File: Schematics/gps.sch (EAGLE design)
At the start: 23 parts, among them IC1 74HC14D, Q1 PE4259, Q2 MIC5365, U1 NEO-8Q, X1 REF_DC, X2 REF_AC

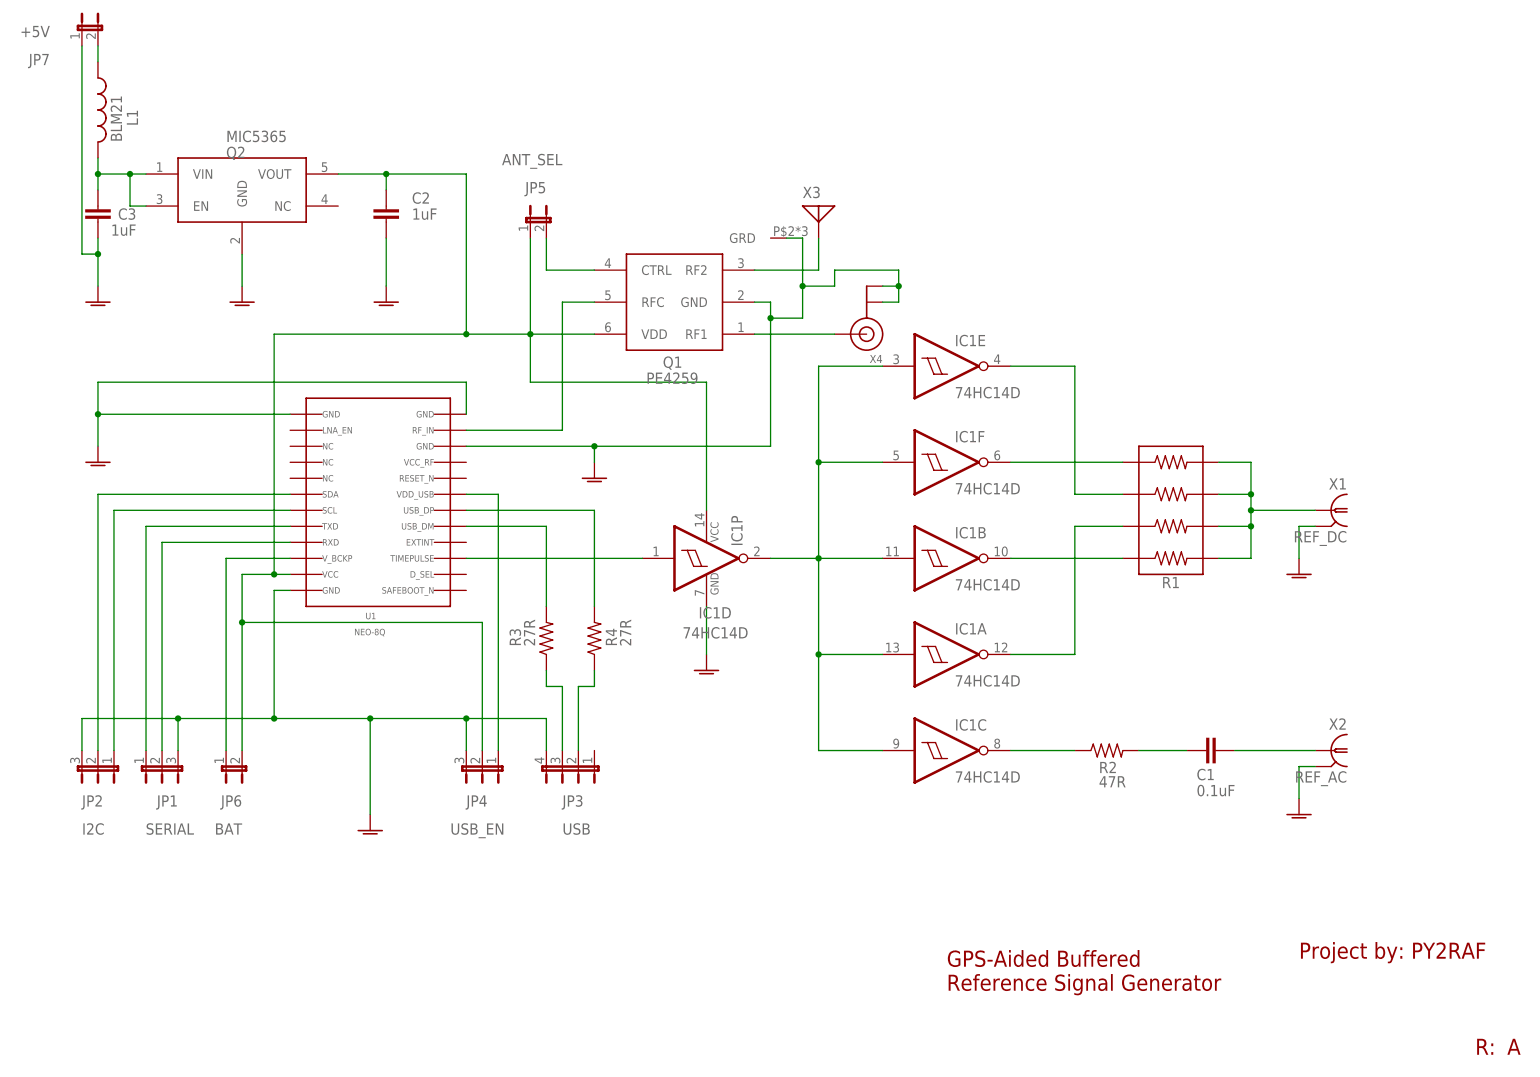
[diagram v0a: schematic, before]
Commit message: New GPS version: Now feeding a Si5351
Test version.
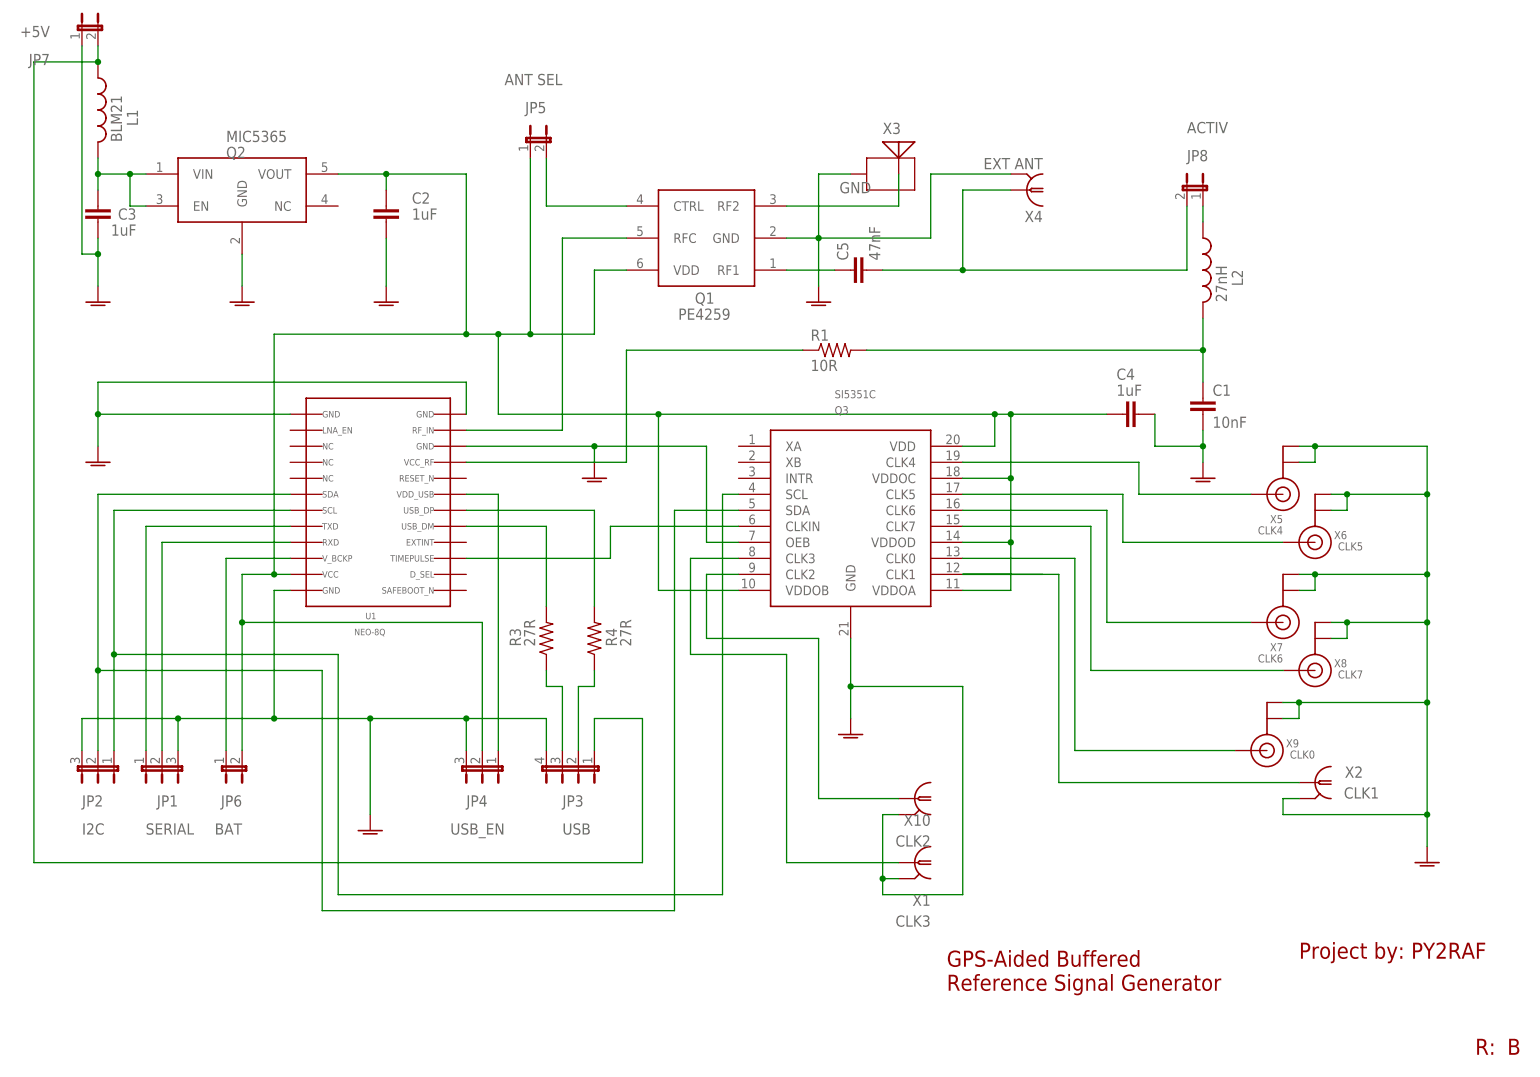
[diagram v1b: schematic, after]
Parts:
- removed IC1: 74HC14D, 74xx-eu:74HC14D
- removed R2: 47R, rcl:R-US_M1206
- added C4: 1uF, rcl:C-EUC1206
- added C5: 47nF, rcl:C-EUC0805K
- added JP8: ACTIV, jumper:JP1E
- added L2: 27nH, aarf:L-0805
- added Q3: SI5351C, aarf:SI5351C
- added X10: CLK2, aarf:SMA-PCB
- added X5: CLK4, adafruit:ANTENNA_U.FL
- added X6: CLK5, adafruit:ANTENNA_U.FL
- added X7: CLK6, adafruit:ANTENNA_U.FL
- added X8: CLK7, adafruit:ANTENNA_U.FL
- added X9: CLK0, adafruit:ANTENNA_U.FL
- C1: value 0.1uF -> 10nF; device rcl:C-EUC1206 -> rcl:C-EUC0805K
- JP5: value ANT_SEL -> ANT SEL
- R1: value (none) -> 10R; device aarf:744C083 -> rcl:R-US_R0805
- X1: value REF_DC -> CLK3
- X2: value REF_AC -> CLK1
- X4: value (none) -> EXT ANT; device adafruit:ANTENNA_U.FL -> aarf:SMA-PCB
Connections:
- removed net N$4: IC1B.O, R1.1
- new net N$28: JP3.1, JP7.2, L1.1
- new net N$29: Q3.CLK7, X8.SIGNAL
- new net N$30: Q3.CLK0, X9.SIGNAL
- new net N$31: Q3.CLK3, X1.1
- net GNDA: now also C1.2, C4.2, Q3.GND, Q3.OEB, X10.2, X4.2, X5.GND@0, X5.GND@1, X6.GND@0, X6.GND@1, X7.GND@0, X7.GND@1, X8.GND@0, X8.GND@1, X9.GND@0, X9.GND@1; no longer IC1P.GND, X4.GND@0, X4.GND@1
- net N$1: now also Q3.CLKIN, U1.P$3; no longer IC1A.I, IC1B.I, IC1C.I, IC1D.O, IC1E.I, IC1F.I
- net N$11: now also JP8.1, L2.1; no longer C1.1, X2.1
- net N$15: now also Q3.SDA
- net N$16: now also Q3.SCL
- net N$2: now also Q3.CLK1, X2.1; no longer IC1E.O, R1.3
- net N$21: now also Q3.CLK4, X5.SIGNAL; no longer R1.5, R1.6, R1.7, R1.8, X1.1
- net N$22: now also C4.1, Q3.VDD, Q3.VDDOA, Q3.VDDOB, Q3.VDDOC, Q3.VDDOD; no longer IC1P.VCC
- net N$25: now also Q3.CLK5, X6.SIGNAL; no longer JP7.2, L1.1
- net N$27: now also Q3.CLK6, X7.SIGNAL; no longer Q1.RF1, X4.SIGNAL
- net N$3: now also Q3.CLK2, X10.1; no longer IC1A.O, R1.2
- net N$5: now also C5.2, JP8.2, X4.1; no longer IC1F.O, R1.4
- net N$6: now also C5.1, Q1.RF1; no longer IC1D.I, U1.P$3
- net N$7: now also R1.1, U1.P$9; no longer IC1C.O, R2.1
- net N$8: now also C1.1, L2.2, R1.2; no longer C1.2, R2.2
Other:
- moved on the sheet: C1, JP5, Q1, X1, X2

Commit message: Rev. B: Pull-up in I2C, new GPS Clock port
* Implemented I²C pull-up resistors (required by datasheet)
* Added a U.FL connector in the GPS clock port that drives the 5351 in
  for test / troubleshoot
* Added schematic, gerber, pictures
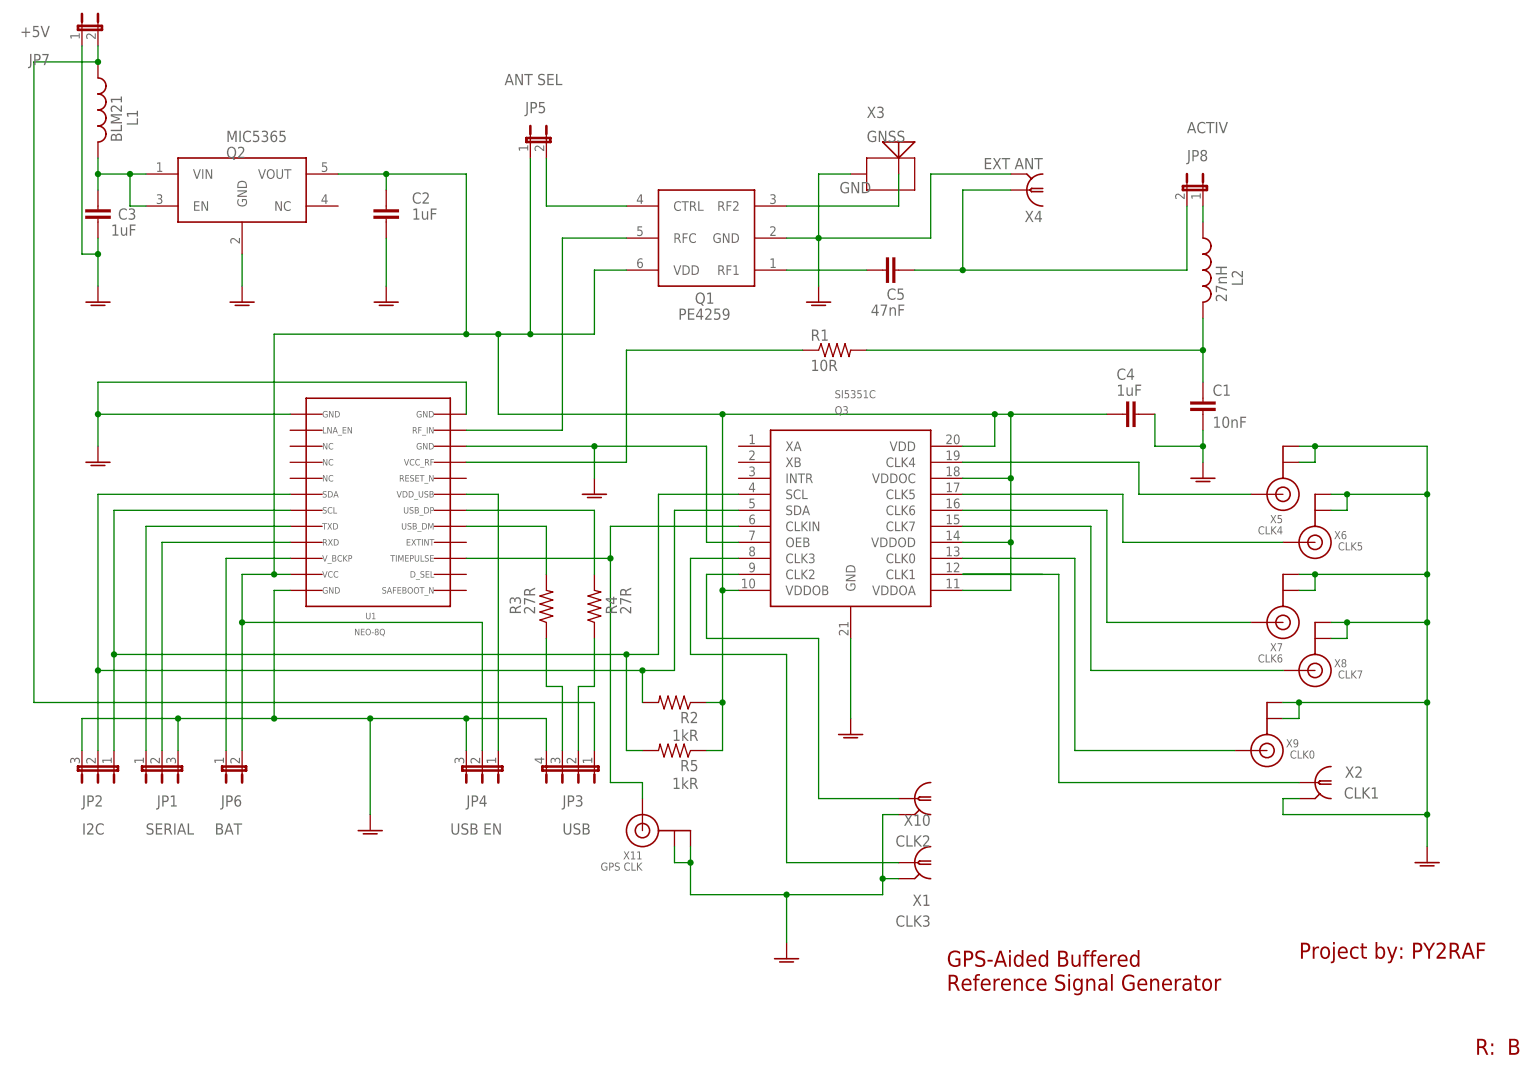
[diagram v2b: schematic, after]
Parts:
- added R2, R5: 1kR, rcl:R-US_R1206
- added X11: GPS CLK, adafruit:ANTENNA_U.FL
- JP4: value USB_EN -> USB EN
- X3: value (none) -> GNSS
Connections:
- net GNDA: now also X11.GND@0, X11.GND@1
- net N$1: now also X11.SIGNAL
- net N$15: now also R2.2
- net N$16: now also R5.2
- net N$22: now also R2.1, R5.1
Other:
- moved on the sheet: C5, R3, R4

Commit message: GPS board: I2C changes
* Separated to two independent I2C ports, one for the uBlox, other for
  the 5351
* Minor re-routing
* Updated BOM, schematics and stuff
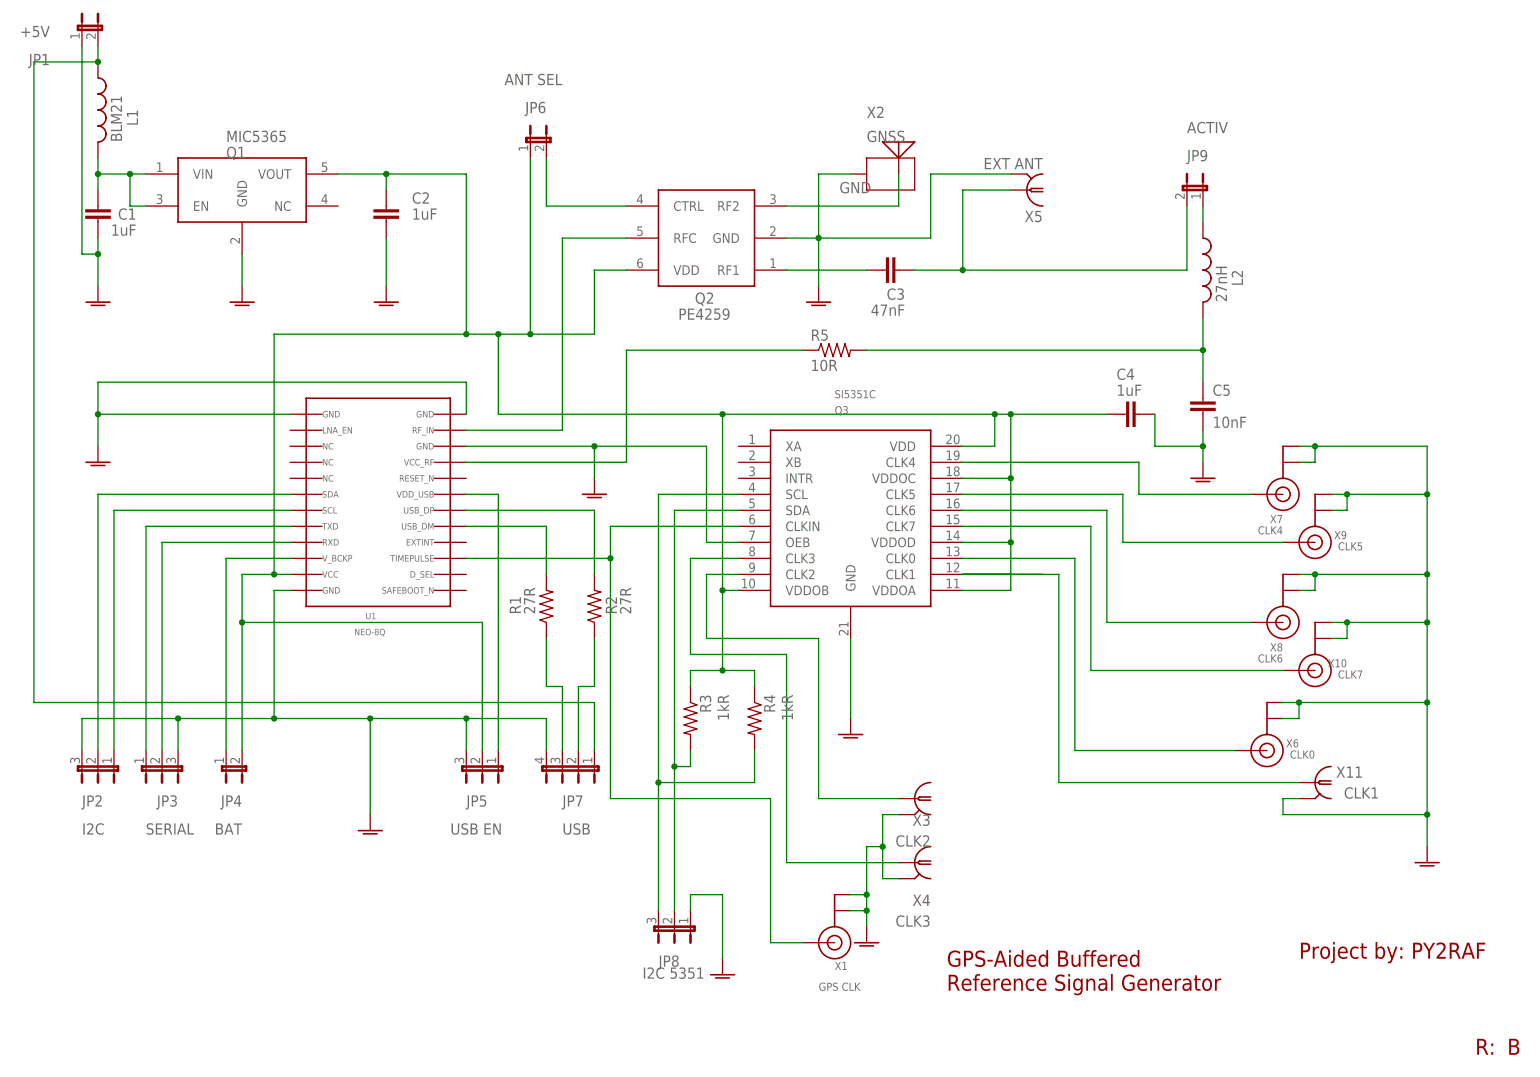
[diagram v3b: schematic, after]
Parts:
- added JP9: ACTIV, jumper:JP1E
- C1: value 10nF -> 1uF; device rcl:C-EUC0805K -> rcl:C-EUC1206
- C3: value 1uF -> 47nF; device rcl:C-EUC1206 -> rcl:C-EUC0805K
- C5: value 47nF -> 10nF
- JP1: value SERIAL -> +5V; device jumper:JP2E -> jumper:JP1E
- JP3: value USB -> SERIAL; device jumper:JP4E -> jumper:JP2E
- JP4: value USB EN -> BAT; device jumper:JP2E -> jumper:JP1E
- JP5: value ANT SEL -> USB EN; device jumper:JP1E -> jumper:JP2E
- JP6: value BAT -> ANT SEL
- JP7: value +5V -> USB; device jumper:JP1E -> jumper:JP4E
- JP8: value ACTIV -> I2C 5351; device jumper:JP1E -> jumper:JP2E
- Q1: value PE4259 -> MIC5365; device aarf:PE4259 -> aarf:MIC5365
- Q2: value MIC5365 -> PE4259; device aarf:MIC5365 -> aarf:PE4259
- R1: value 10R -> 27R; device rcl:R-US_R0805 -> rcl:R-US_M1206
- R2: value 1kR -> 27R; device rcl:R-US_R1206 -> rcl:R-US_M1206
- R3, R4: value 27R -> 1kR; device rcl:R-US_M1206 -> rcl:R-US_R1206
- R5: value 1kR -> 10R; device rcl:R-US_R1206 -> rcl:R-US_R0805
- X1: value CLK3 -> GPS CLK; device aarf:SMA-PCB -> adafruit:ANTENNA_U.FL
- X10: value CLK2 -> CLK7; device aarf:SMA-PCB -> adafruit:ANTENNA_U.FL
- X11: value GPS CLK -> CLK1; device adafruit:ANTENNA_U.FL -> aarf:SMA-PCB
- X2: value CLK1 -> GNSS; device aarf:SMA-PCB -> aarf:ANT-GNSS-MLX
- X3: value GNSS -> CLK2; device aarf:ANT-GNSS-MLX -> aarf:SMA-PCB
- X4: value EXT ANT -> CLK3
- X5: value CLK4 -> EXT ANT; device adafruit:ANTENNA_U.FL -> aarf:SMA-PCB
- X6: value CLK5 -> CLK0
- X7: value CLK6 -> CLK4
- X8: value CLK7 -> CLK6
- X9: value CLK0 -> CLK5
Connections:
- new net N$32: JP8.2, Q3.SDA, R3.2
- new net N$4: JP8.3, Q3.SCL, R4.2
- net GNDA: now also C5.2, JP1.1, JP3.3, JP5.3, JP7.4, JP8.1, X1.GND@0, X1.GND@1, X10.GND@0, X10.GND@1, X11.2, X2.GRD, X3.2, X5.2; no longer C3.2, JP1.3, JP3.4, JP4.3, JP7.1, X1.2, X10.2, X11.GND@0, X11.GND@1, X2.2, X3.GRD, X5.GND@0, X5.GND@1
- net N$1: now also X1.SIGNAL; no longer X11.SIGNAL
- net N$10: now also R2.2; no longer R4.2
- net N$11: now also JP9.1; no longer JP8.1
- net N$12: now also JP5.1; no longer JP4.1
- net N$13: now also JP7.3, R1.1; no longer JP3.3, R3.1
- net N$14: now also JP7.2, R2.1; no longer JP3.2, R4.1
- net N$15: no longer Q3.SDA, R2.2
- net N$16: no longer Q3.SCL, R5.2
- net N$17: now also JP3.2; no longer JP1.2
- net N$18: now also JP3.1; no longer JP1.1
- net N$19: now also JP4.1; no longer JP6.1
- net N$2: now also X11.1; no longer X2.1
- net N$20: now also JP6.2, Q2.CTRL; no longer JP5.2, Q1.CTRL
- net N$21: now also X7.SIGNAL; no longer X5.SIGNAL
- net N$22: now also JP5.2, JP6.1, Q1.VOUT, Q2.VDD, R3.1, R4.1; no longer JP5.1, JP6.2, Q1.VDD, Q2.VOUT, R2.1, R5.1
- net N$23: now also Q2.RFC; no longer Q1.RFC
- net N$24: now also C1.1, Q1.EN, Q1.VIN; no longer C3.1, Q2.EN, Q2.VIN
- net N$25: now also X9.SIGNAL; no longer X6.SIGNAL
- net N$26: now also Q2.RF2, X2.ANT; no longer Q1.RF2, X3.ANT
- net N$27: now also X8.SIGNAL; no longer X7.SIGNAL
- net N$28: now also JP1.2, JP7.1; no longer JP3.1, JP7.2
- net N$29: now also X10.SIGNAL; no longer X8.SIGNAL
- net N$3: now also X3.1; no longer X10.1
- net N$30: now also X6.SIGNAL; no longer X9.SIGNAL
- net N$31: now also X4.1; no longer X1.1
- net N$5: now also C3.2, JP9.2, X5.1; no longer C5.2, JP8.2, X4.1
- net N$6: now also C3.1, Q2.RF1; no longer C5.1, Q1.RF1
- net N$7: now also R5.1; no longer R1.1
- net N$8: now also C5.1, R5.2; no longer C1.1, R1.2
- net N$9: now also R1.2; no longer R3.2
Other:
- moved on the sheet: C1, C3, C5, JP6, R1, R2, R3, R4, R5, X4, X6, X7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

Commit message: Sync-up
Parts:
- L2: device aarf:L-0805 -> aarf:L-0603
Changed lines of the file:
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@@
 <part name="C3" library="rcl" library_urn="urn:adsk.eagle:library:334" deviceset="C-EU" device="C0805K" package3d_urn="urn:adsk.eagle:package:23681/2" value="47nF"/>
 <part name="GND11" library="supply1" library_urn="urn:adsk.eagle:library:371" deviceset="GNDA" device=""/>
-<part name="L2" library="aarf" deviceset="L-0805" device="" value="27nH"/>
+<part name="L2" library="aarf" deviceset="L-0603" device="" value="27nH"/>
 <part name="X7" library="adafruit" deviceset="ANTENNA_U.FL" device="" value="CLK4"/>
 <part name="X9" library="adafruit" deviceset="ANTENNA_U.FL" device="" value="CLK5"/>
